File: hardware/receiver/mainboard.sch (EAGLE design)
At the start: 16 parts, among them J2 POWER_JACKPTH, J3 AVR_SPI_PRG_6PTH, Q1 MOSFET-NCHANNELAO3404A, U1 ATMEGA328P_TQFP, U2 RFM69HCW

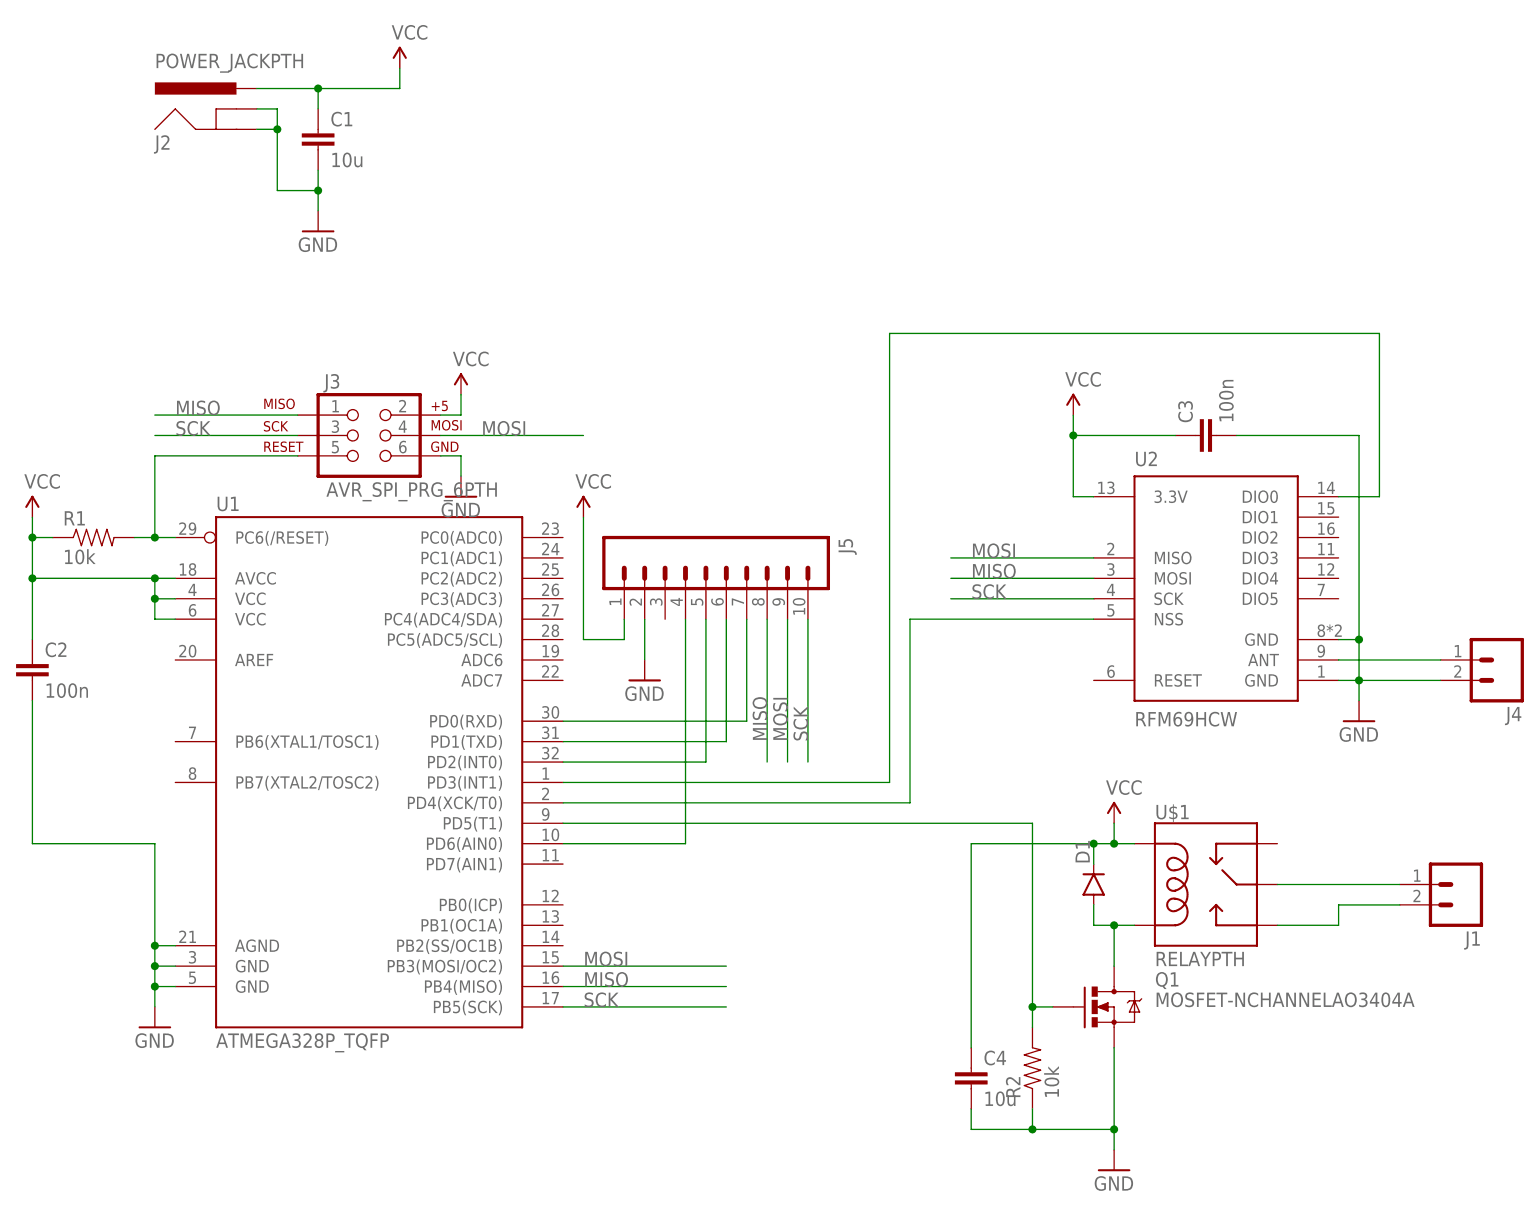
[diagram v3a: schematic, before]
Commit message: Added BOM and diode protection
Receiver
* Added BOM
* Issue with relay activation voltage
 * Had to change VIN to 5V and add a regulator to 3.3B
 * Added VIN pin to expansion header
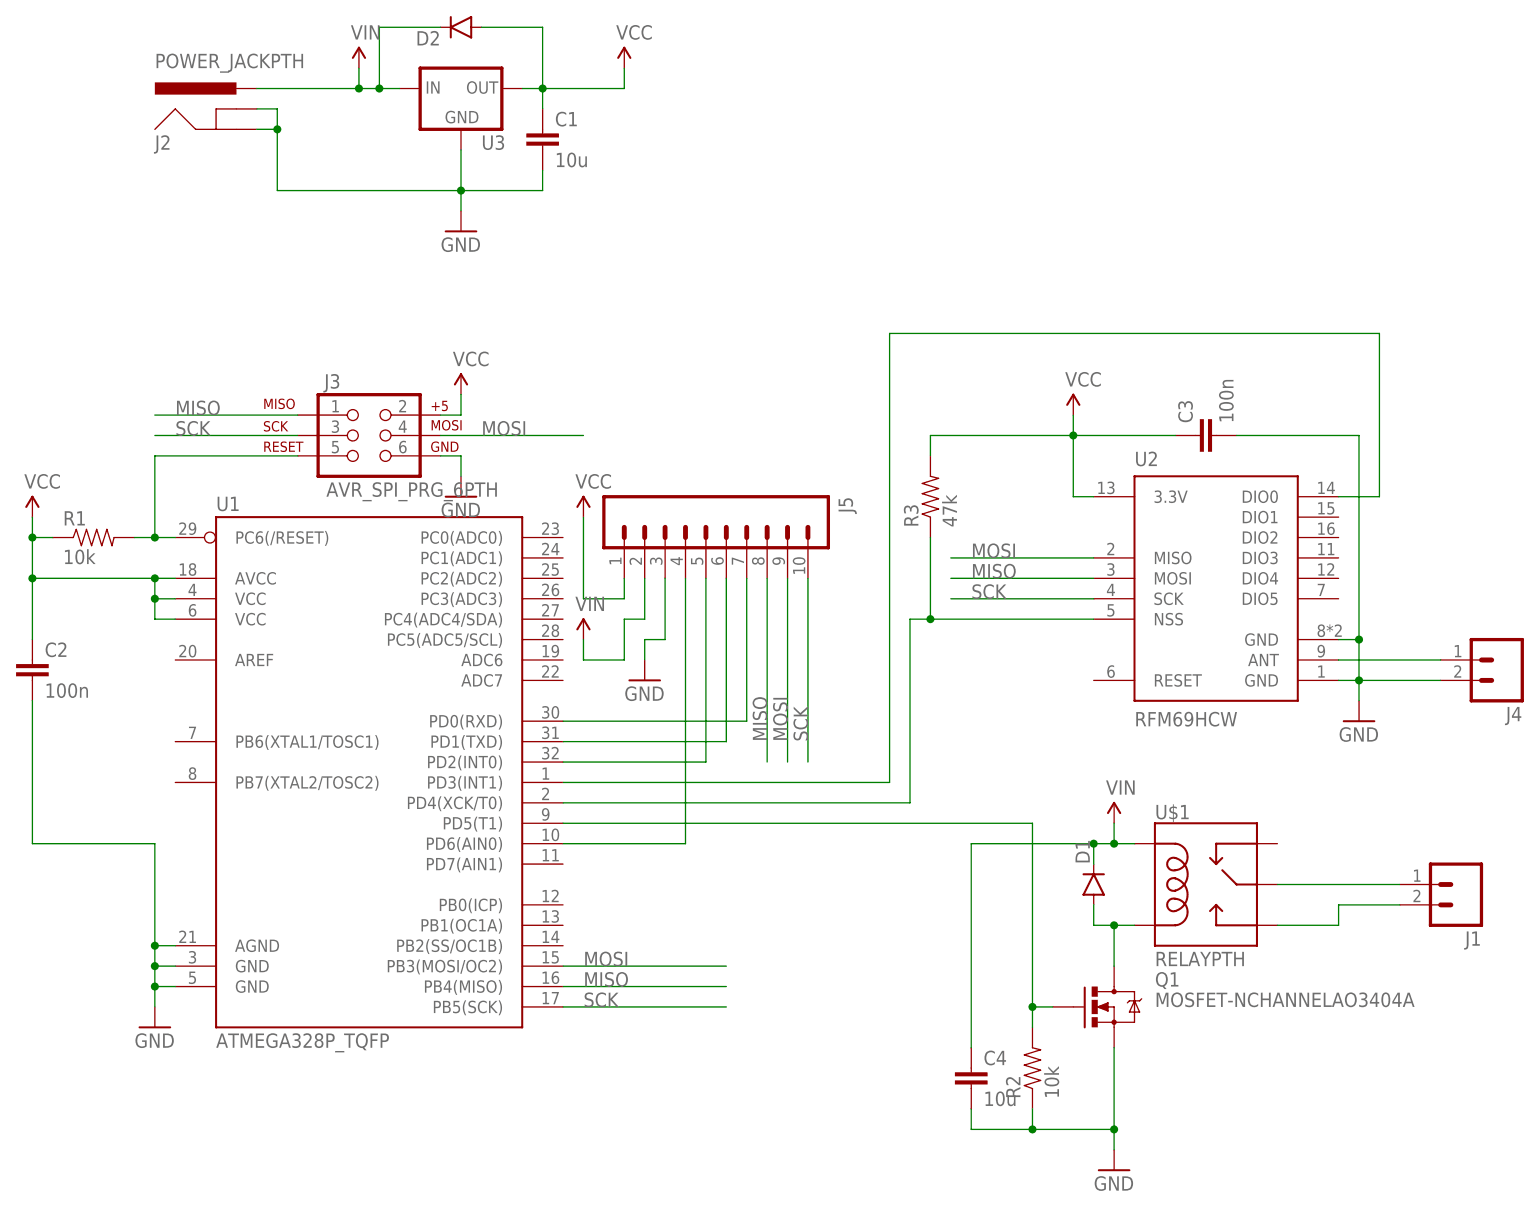
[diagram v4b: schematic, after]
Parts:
- added D2: (no value), SparkFun-DiscreteSemi:DIODEBAS16
- added R3: 47k, SparkFun-Passives:RESISTOR0603-RES
- added U3: (no value), SparkFun-PowerIC:V_REG_78XXTO-92_UNTESTED
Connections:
- new net VIN: C4.1, D1.C, D2.C, J2.PWR, J5.2, U$1.COIL1, U3.IN
- net GND: now also J5.3, U3.GND; no longer J5.2
- net N$1: now also R3.1
- net VCC: now also D2.A, R3.2, U3.OUT; no longer C4.1, D1.C, J2.PWR, U$1.COIL1
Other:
- moved on the sheet: C1, J5

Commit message: Initial PCB layout of Receiver
Receiver
* Changed expansion connector pinout to make layout easier
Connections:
- net MISO: now also J5.10; no longer J5.8
- net MOSI: now also J5.8; no longer J5.9
- net N$11: now also U1.PD0(RXD); no longer U1.PD2(INT0)
- net N$9: now also U1.PD2(INT0); no longer U1.PD0(RXD)
- net SCK: now also J5.9; no longer J5.10
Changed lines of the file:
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@@
 </segment>
 <segment>
-<pinref part="J5" gate="G$1" pin="9"/>
-<wire x1="127" y1="45.72" x2="127" y2="22.86" width="0.1524" layer="91"/>
-<label x="127" y="25.4" size="1.778" layer="95" rot="R90"/>
+<pinref part="J5" gate="G$1" pin="8"/>
+<wire x1="124.46" y1="45.72" x2="124.46" y2="22.86" width="0.1524" layer="91"/>
+<label x="124.46" y="25.4" size="1.778" layer="95" rot="R90"/>
 </segment>
 </net>
@@
 </segment>
 <segment>
-<pinref part="J5" gate="G$1" pin="10"/>
-<wire x1="129.54" y1="45.72" x2="129.54" y2="22.86" width="0.1524" layer="91"/>
-<label x="129.54" y="25.4" size="1.778" layer="95" rot="R90"/>
+<pinref part="J5" gate="G$1" pin="9"/>
+<wire x1="127" y1="45.72" x2="127" y2="22.86" width="0.1524" layer="91"/>
+<label x="127" y="25.4" size="1.778" layer="95" rot="R90"/>
 </segment>
 </net>
@@
 </segment>
 <segment>
-<pinref part="J5" gate="G$1" pin="8"/>
-<wire x1="124.46" y1="45.72" x2="124.46" y2="22.86" width="0.1524" layer="91"/>
-<label x="124.46" y="25.4" size="1.778" layer="95" rot="R90"/>
+<pinref part="J5" gate="G$1" pin="10"/>
+<wire x1="129.54" y1="45.72" x2="129.54" y2="22.86" width="0.1524" layer="91"/>
+<label x="129.54" y="25.4" size="1.778" layer="95" rot="R90"/>
 </segment>
 </net>
@@
 </segment>
 </net>
-<net name="N$9" class="0">
-<segment>
-<pinref part="J5" gate="G$1" pin="7"/>
-<wire x1="121.92" y1="45.72" x2="121.92" y2="27.94" width="0.1524" layer="91"/>
-<pinref part="U1" gate="U$1" pin="PD0(RXD)"/>
-<wire x1="121.92" y1="27.94" x2="99.06" y2="27.94" width="0.1524" layer="91"/>
-</segment>
-</net>
-<net name="N$10" class="0">
-<segment>
-<pinref part="U1" gate="U$1" pin="PD1(TXD)"/>
-<pinref part="J5" gate="G$1" pin="6"/>
-<wire x1="99.06" y1="25.4" x2="119.38" y2="25.4" width="0.1524" layer="91"/>
-<wire x1="119.38" y1="25.4" x2="119.38" y2="45.72" width="0.1524" layer="91"/>
-</segment>
-</net>
-<net name="N$11" class="0">
-<segment>
-<pinref part="U1" gate="U$1" pin="PD2(INT0)"/>
-<pinref part="J5" gate="G$1" pin="5"/>
-<wire x1="99.06" y1="22.86" x2="116.84" y2="22.86" width="0.1524" layer="91"/>
-<wire x1="116.84" y1="22.86" x2="116.84" y2="45.72" width="0.1524" layer="91"/>
-</segment>
-</net>
 <net name="VIN" class="0">
 <segment>
@@
 </segment>
 </net>
+<net name="N$9" class="0">
+<segment>
+<pinref part="U1" gate="U$1" pin="PD2(INT0)"/>
+<pinref part="J5" gate="G$1" pin="7"/>
+<wire x1="99.06" y1="22.86" x2="121.92" y2="22.86" width="0.1524" layer="91"/>
+<wire x1="121.92" y1="22.86" x2="121.92" y2="45.72" width="0.1524" layer="91"/>
+</segment>
+</net>
+<net name="N$10" class="0">
+<segment>
+<pinref part="J5" gate="G$1" pin="6"/>
+<wire x1="119.38" y1="45.72" x2="119.38" y2="25.4" width="0.1524" layer="91"/>
+<pinref part="U1" gate="U$1" pin="PD1(TXD)"/>
+<wire x1="119.38" y1="25.4" x2="99.06" y2="25.4" width="0.1524" layer="91"/>
+</segment>
+</net>
+<net name="N$11" class="0">
+<segment>
+<pinref part="U1" gate="U$1" pin="PD0(RXD)"/>
+<pinref part="J5" gate="G$1" pin="5"/>
+<wire x1="99.06" y1="27.94" x2="116.84" y2="27.94" width="0.1524" layer="91"/>
+<wire x1="116.84" y1="27.94" x2="116.84" y2="45.72" width="0.1524" layer="91"/>
+</segment>
+</net>

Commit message: Fixed SPI mismatch
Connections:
- net MISO: now also U2.MISO; no longer U2.MOSI
- net MOSI: now also U2.MOSI; no longer U2.MISO
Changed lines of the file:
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@@
+</segment>
+<segment>
+<pinref part="U1" gate="U$1" pin="PB3(MOSI/OC2)"/>
+<wire x1="99.06" y1="-2.54" x2="119.38" y2="-2.54" width="0.1524" layer="91"/>
+<label x="101.6" y="-2.54" size="1.778" layer="95"/>
+</segment>
+<segment>
+<pinref part="J5" gate="G$1" pin="8"/>
+<wire x1="124.46" y1="45.72" x2="124.46" y2="22.86" width="0.1524" layer="91"/>
+<label x="124.46" y="25.4" size="1.778" layer="95" rot="R90"/>
+</segment>
+<segment>
+<pinref part="U2" gate="G$1" pin="MOSI"/>
+<wire x1="165.1" y1="45.72" x2="147.32" y2="45.72" width="0.1524" layer="91"/>
+<label x="149.86" y="45.72" size="1.778" layer="95"/>
+</segment>
+</net>
+<net name="SCK" class="0">
+<segment>
+<pinref part="J3" gate="G$1" pin="3"/>
+<wire x1="66.04" y1="63.5" x2="48.26" y2="63.5" width="0.1524" layer="91"/>
+<label x="50.8" y="63.5" size="1.778" layer="95"/>
+</segment>
+<segment>
+<pinref part="U2" gate="G$1" pin="SCK"/>
+<wire x1="165.1" y1="43.18" x2="147.32" y2="43.18" width="0.1524" layer="91"/>
+<label x="149.86" y="43.18" size="1.778" layer="95"/>
+</segment>
+<segment>
+<pinref part="U1" gate="U$1" pin="PB5(SCK)"/>
+<wire x1="99.06" y1="-7.62" x2="119.38" y2="-7.62" width="0.1524" layer="91"/>
+<label x="101.6" y="-7.62" size="1.778" layer="95"/>
+</segment>
+<segment>
+<pinref part="J5" gate="G$1" pin="9"/>
+<wire x1="127" y1="45.72" x2="127" y2="22.86" width="0.1524" layer="91"/>
+<label x="127" y="25.4" size="1.778" layer="95" rot="R90"/>
+</segment>
+</net>
+<net name="MISO" class="0">
+<segment>
+<pinref part="J3" gate="G$1" pin="1"/>
+<wire x1="66.04" y1="66.04" x2="48.26" y2="66.04" width="0.1524" layer="91"/>
+<label x="50.8" y="66.04" size="1.778" layer="95"/>
+</segment>
+<segment>
+<pinref part="U1" gate="U$1" pin="PB4(MISO)"/>
+<wire x1="99.06" y1="-5.08" x2="119.38" y2="-5.08" width="0.1524" layer="91"/>
+<label x="101.6" y="-5.08" size="1.778" layer="95"/>
+</segment>
+<segment>
+<pinref part="J5" gate="G$1" pin="10"/>
+<wire x1="129.54" y1="45.72" x2="129.54" y2="22.86" width="0.1524" layer="91"/>
+<label x="129.54" y="25.4" size="1.778" layer="95" rot="R90"/>
 </segment>
 <segment>
@@
 <wire x1="165.1" y1="48.26" x2="147.32" y2="48.26" width="0.1524" layer="91"/>
 <label x="149.86" y="48.26" size="1.778" layer="95"/>
-</segment>
-<segment>
-<pinref part="U1" gate="U$1" pin="PB3(MOSI/OC2)"/>
-<wire x1="99.06" y1="-2.54" x2="119.38" y2="-2.54" width="0.1524" layer="91"/>
-<label x="101.6" y="-2.54" size="1.778" layer="95"/>
-</segment>
-<segment>
-<pinref part="J5" gate="G$1" pin="8"/>
-<wire x1="124.46" y1="45.72" x2="124.46" y2="22.86" width="0.1524" layer="91"/>
-<label x="124.46" y="25.4" size="1.778" layer="95" rot="R90"/>
-</segment>
-</net>
-<net name="SCK" class="0">
-<segment>
-<pinref part="J3" gate="G$1" pin="3"/>
-<wire x1="66.04" y1="63.5" x2="48.26" y2="63.5" width="0.1524" layer="91"/>
-<label x="50.8" y="63.5" size="1.778" layer="95"/>
-</segment>
-<segment>
-<pinref part="U2" gate="G$1" pin="SCK"/>
-<wire x1="165.1" y1="43.18" x2="147.32" y2="43.18" width="0.1524" layer="91"/>
-<label x="149.86" y="43.18" size="1.778" layer="95"/>
-</segment>
-<segment>
-<pinref part="U1" gate="U$1" pin="PB5(SCK)"/>
-<wire x1="99.06" y1="-7.62" x2="119.38" y2="-7.62" width="0.1524" layer="91"/>
-<label x="101.6" y="-7.62" size="1.778" layer="95"/>
-</segment>
-<segment>
-<pinref part="J5" gate="G$1" pin="9"/>
-<wire x1="127" y1="45.72" x2="127" y2="22.86" width="0.1524" layer="91"/>
-<label x="127" y="25.4" size="1.778" layer="95" rot="R90"/>
-</segment>
-</net>
-<net name="MISO" class="0">
-<segment>
-<pinref part="J3" gate="G$1" pin="1"/>
-<wire x1="66.04" y1="66.04" x2="48.26" y2="66.04" width="0.1524" layer="91"/>
-<label x="50.8" y="66.04" size="1.778" layer="95"/>
-</segment>
-<segment>
-<pinref part="U2" gate="G$1" pin="MOSI"/>
-<wire x1="165.1" y1="45.72" x2="147.32" y2="45.72" width="0.1524" layer="91"/>
-<label x="149.86" y="45.72" size="1.778" layer="95"/>
-</segment>
-<segment>
-<pinref part="U1" gate="U$1" pin="PB4(MISO)"/>
-<wire x1="99.06" y1="-5.08" x2="119.38" y2="-5.08" width="0.1524" layer="91"/>
-<label x="101.6" y="-5.08" size="1.778" layer="95"/>
-</segment>
-<segment>
-<pinref part="J5" gate="G$1" pin="10"/>
-<wire x1="129.54" y1="45.72" x2="129.54" y2="22.86" width="0.1524" layer="91"/>
-<label x="129.54" y="25.4" size="1.778" layer="95" rot="R90"/>
 </segment>
 </net>
@@
 </sheet>
 </sheets>
+<errors>
+</errors>
 </schematic>
 </drawing>

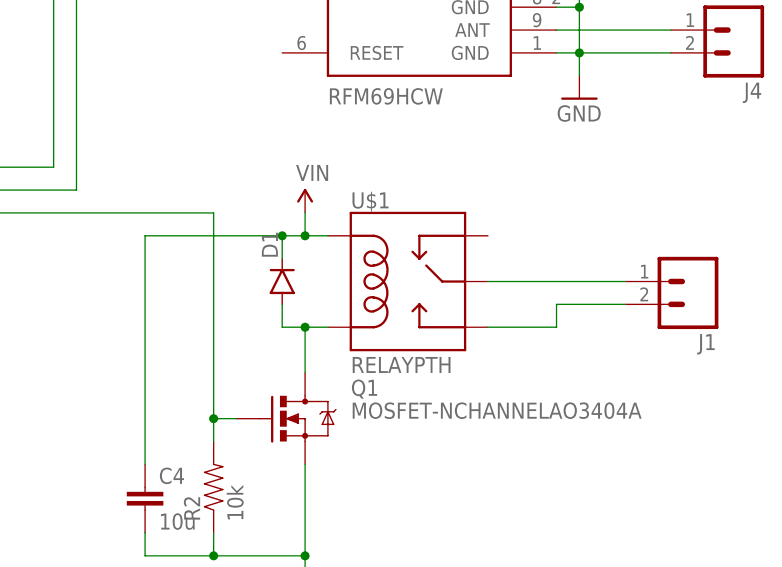
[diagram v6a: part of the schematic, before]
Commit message: Replaced relay and voltage regulator in schematic
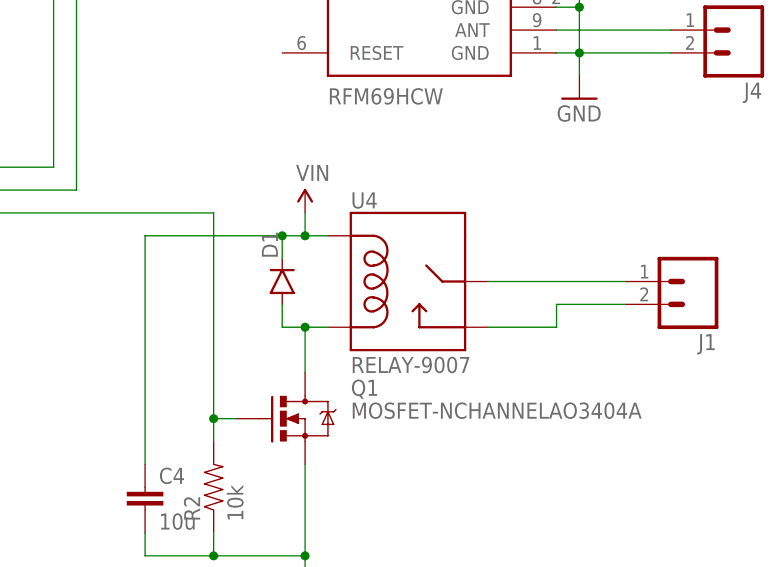
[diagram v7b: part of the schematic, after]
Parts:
- removed U$1: RELAYPTH, SparkFun-Electromechanical:RELAYPTH
- added U4: RELAY-9007, Electromechanical:RELAY-9007
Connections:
- net N$5: now also U4.MAIN; no longer U$1.MAIN
- net N$6: now also U4.NO; no longer U$1.NO
- net N$7: now also U4.COIL2; no longer U$1.COIL2
- net VIN: now also U4.COIL1; no longer U$1.COIL1
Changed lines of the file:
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@@
 <part name="U1" library="SparkFun-DigitalIC" deviceset="ATMEGA328P_TQFP" device="" value="ATMEGA328P_TQFP"/>
 <part name="U2" library="SparkFun-RF" deviceset="RFM69H" device="CW"/>
-<part name="U$1" library="SparkFun-Electromechanical" deviceset="RELAY" device="PTH"/>
 <part name="J1" library="SparkFun-Connectors" deviceset="M02" device="5MM"/>
 <part name="J2" library="SparkFun-Connectors" deviceset="POWER_JACK" device="PTH"/>
@@
 <part name="D2" library="SparkFun-DiscreteSemi" deviceset="DIODE" device="BAS16"/>
 <part name="SUPPLY5" library="SparkFun-Aesthetics" deviceset="VIN" device=""/>
+<part name="U4" library="Electromechanical" deviceset="RELAY-9007" device=""/>
 </parts>
 <sheets>
@@
 <instance part="U1" gate="U$1" x="76.2" y="20.32"/>
 <instance part="U2" gate="G$1" x="180.34" y="43.18"/>
-<instance part="U$1" gate="K$1" x="180.34" y="7.62"/>
 <instance part="J1" gate="G$1" x="210.82" y="7.62" rot="R180"/>
 <instance part="J2" gate="G$1" x="58.42" y="99.06"/>
@@
 <instance part="D2" gate="G$1" x="86.36" y="114.3" rot="R180"/>
 <instance part="SUPPLY5" gate="G$1" x="101.6" y="38.1"/>
+<instance part="U4" gate="G$1" x="180.34" y="7.62"/>
 </instances>
 <busses>
@@
 </segment>
 </net>
-<net name="N$5" class="0">
-<segment>
-<pinref part="U$1" gate="K$1" pin="MAIN"/>
-<pinref part="J1" gate="G$1" pin="1"/>
-<wire x1="187.96" y1="7.62" x2="203.2" y2="7.62" width="0.1524" layer="91"/>
-</segment>
-</net>
 <net name="N$6" class="0">
 <segment>
@@
 <wire x1="203.2" y1="5.08" x2="195.58" y2="5.08" width="0.1524" layer="91"/>
 <wire x1="195.58" y1="5.08" x2="195.58" y2="2.54" width="0.1524" layer="91"/>
-<pinref part="U$1" gate="K$1" pin="NO"/>
+<pinref part="U4" gate="G$1" pin="NO"/>
 <wire x1="195.58" y1="2.54" x2="187.96" y2="2.54" width="0.1524" layer="91"/>
 </segment>
@@
 <pinref part="Q1" gate="G$1" pin="D"/>
 <wire x1="167.64" y1="-2.54" x2="167.64" y2="2.54" width="0.1524" layer="91"/>
-<pinref part="U$1" gate="K$1" pin="COIL2"/>
-<wire x1="167.64" y1="2.54" x2="170.18" y2="2.54" width="0.1524" layer="91"/>
 <pinref part="D1" gate="G$1" pin="A"/>
 <wire x1="165.1" y1="5.08" x2="165.1" y2="2.54" width="0.1524" layer="91"/>
 <wire x1="165.1" y1="2.54" x2="167.64" y2="2.54" width="0.1524" layer="91"/>
+<pinref part="U4" gate="G$1" pin="COIL2"/>
+<wire x1="170.18" y1="2.54" x2="167.64" y2="2.54" width="0.1524" layer="91"/>
 <junction x="167.64" y="2.54"/>
 </segment>
@@
 </segment>
 <segment>
-<pinref part="U$1" gate="K$1" pin="COIL1"/>
 <pinref part="D1" gate="G$1" pin="C"/>
 <wire x1="165.1" y1="10.16" x2="165.1" y2="12.7" width="0.1524" layer="91"/>
 <wire x1="165.1" y1="12.7" x2="167.64" y2="12.7" width="0.1524" layer="91"/>
 <pinref part="C4" gate="G$1" pin="1"/>
-<wire x1="167.64" y1="12.7" x2="170.18" y2="12.7" width="0.1524" layer="91"/>
 <wire x1="149.86" y1="-12.7" x2="149.86" y2="12.7" width="0.1524" layer="91"/>
 <wire x1="149.86" y1="12.7" x2="165.1" y2="12.7" width="0.1524" layer="91"/>
@@
 <pinref part="SUPPLY8" gate="G$1" pin="VIN"/>
 <wire x1="167.64" y1="15.24" x2="167.64" y2="12.7" width="0.1524" layer="91"/>
+<pinref part="U4" gate="G$1" pin="COIL1"/>
+<wire x1="170.18" y1="12.7" x2="167.64" y2="12.7" width="0.1524" layer="91"/>
 <junction x="167.64" y="12.7"/>
 </segment>
@@
 </segment>
 </net>
+<net name="N$5" class="0">
+<segment>
+<pinref part="U4" gate="G$1" pin="MAIN"/>
+<pinref part="J1" gate="G$1" pin="1"/>
+<wire x1="187.96" y1="7.62" x2="203.2" y2="7.62" width="0.1524" layer="91"/>
+</segment>
+</net>
